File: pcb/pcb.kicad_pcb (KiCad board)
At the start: 2 copper layers, 109 x 54 mm, 60 parts, among them J1 MALE, J10 TC2030_NL, J101 MALE, J102 FEMALE, J103 MALE, J104 FEMALE, J105 MALE, J106 FEMALE, J107 MALE, J108 FEMALE, J11 STANDOFF, J111 STANDOFF, J112 STANDOFF, J113 STANDOFF, J114 STANDOFF, J12 STANDOFF, J13 STANDOFF, J14 STANDOFF, J2 FEMALE, J3 MALE, J4 FEMALE, J5 MALE, J6 FEMALE, J7 MALE, J8 FEMALE, J9 DTR, Q1 2N3904, SW1 ACTION, SW2 ACTION, SW3 ACTION, SW4 ACTION, U3 ATmega328P-MU, Y1 YSX321SL

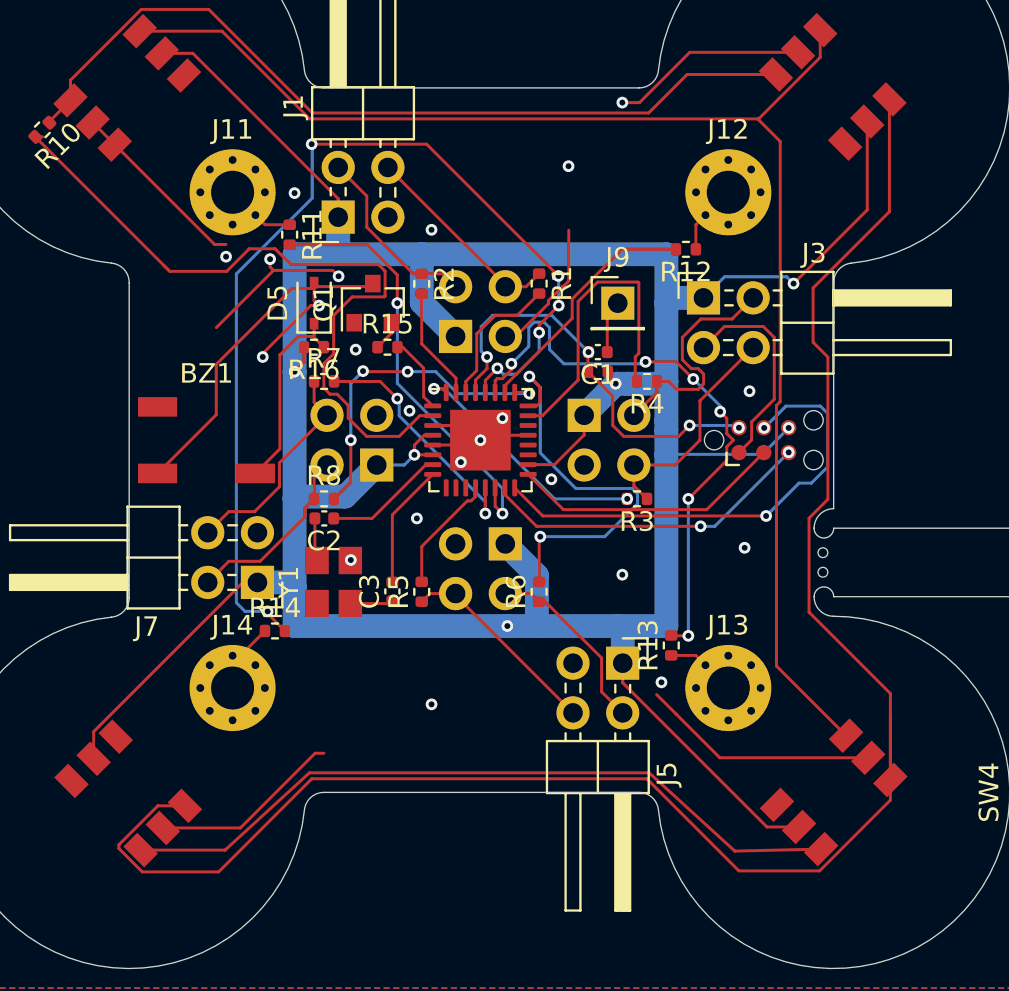
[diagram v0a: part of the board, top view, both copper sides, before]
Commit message: Fix: Tag-Connect cannot be pushed through holes
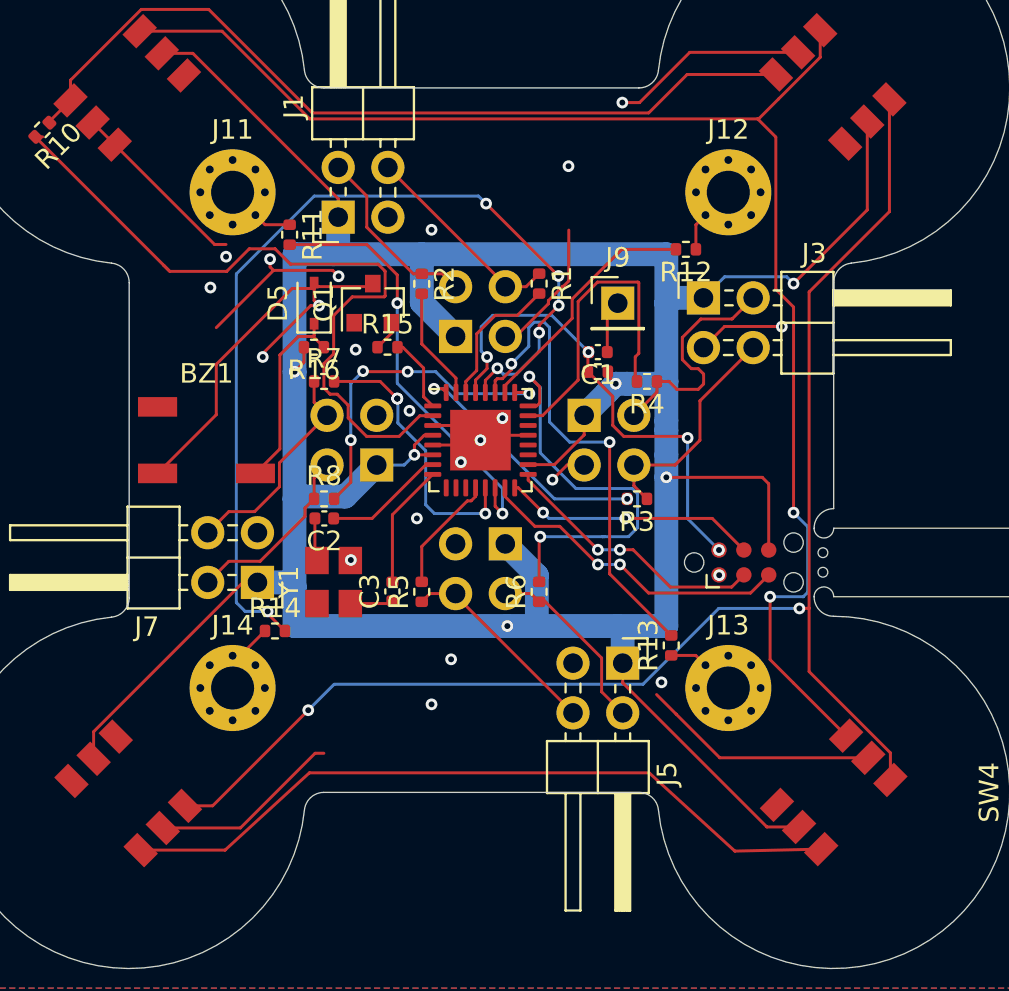
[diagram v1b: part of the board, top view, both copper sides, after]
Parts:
- moved J10 6.33 mm to (134.5, 111.2)
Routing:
- net Net-(D2-Pad3): track 92.9 -> 74.3 mm, vias 0 -> 2
- net /Bottom/MISO: track 24.2 -> 13.0 mm
- net Net-(R13-Pad2): track 30.5 -> 25.0 mm, vias 6 -> 2
- net GNDB: track 75.5 -> 71.0 mm, vias 19 -> 20
- net Net-(R14-Pad2): track 52.1 -> 48.3 mm
- net /Bottom/~RST: track 21.5 -> 25.0 mm
- net Net-(D1-Pad3): track 72.9 -> 75.3 mm, vias 0 -> 2
- net +5VB: track 175.7 -> 177.6 mm
- net Net-(R7-Pad2): track 12.6 -> 14.3 mm, vias 2 -> 3
- net Net-(R6-Pad2): track 20.7 -> 21.5 mm
- net /Bottom/MOSI: track 17.1 -> 16.3 mm
- net /Bottom/SCK: track 14.0 -> 13.8 mm, vias 0 -> 2
- net Net-(J11-Pad1): vias 1 -> 0

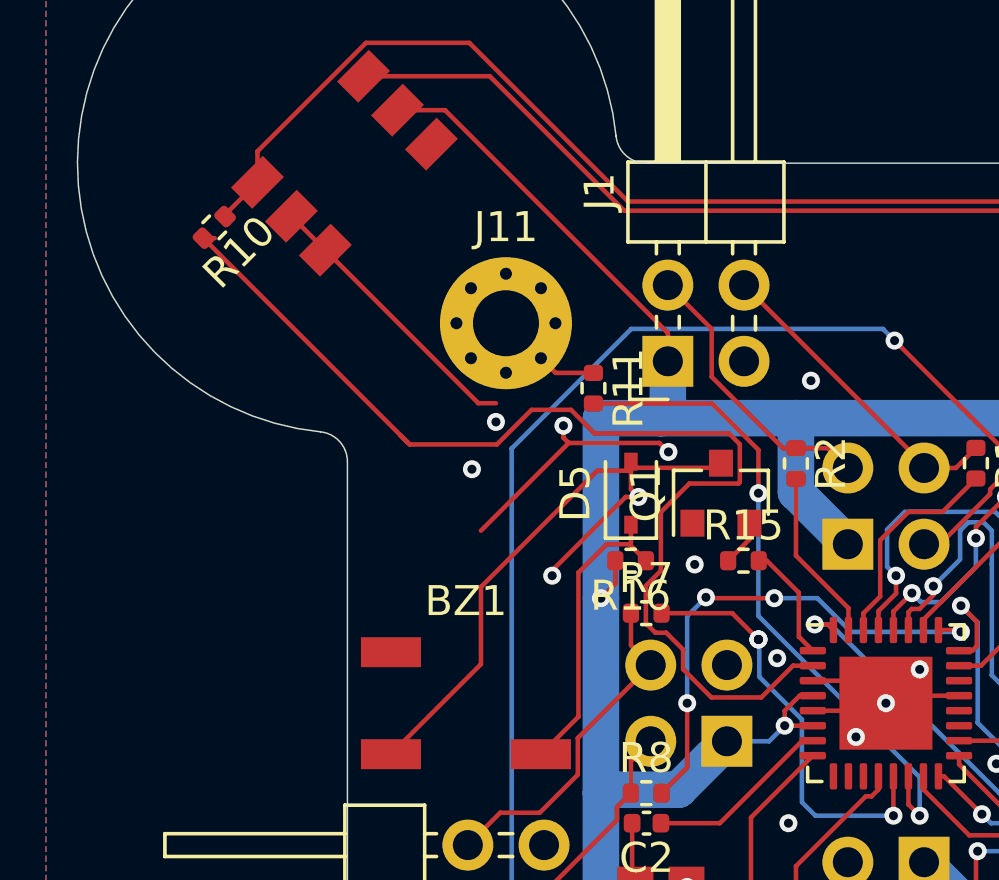
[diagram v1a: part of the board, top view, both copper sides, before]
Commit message: Fix: Small resistor not in solder mask area
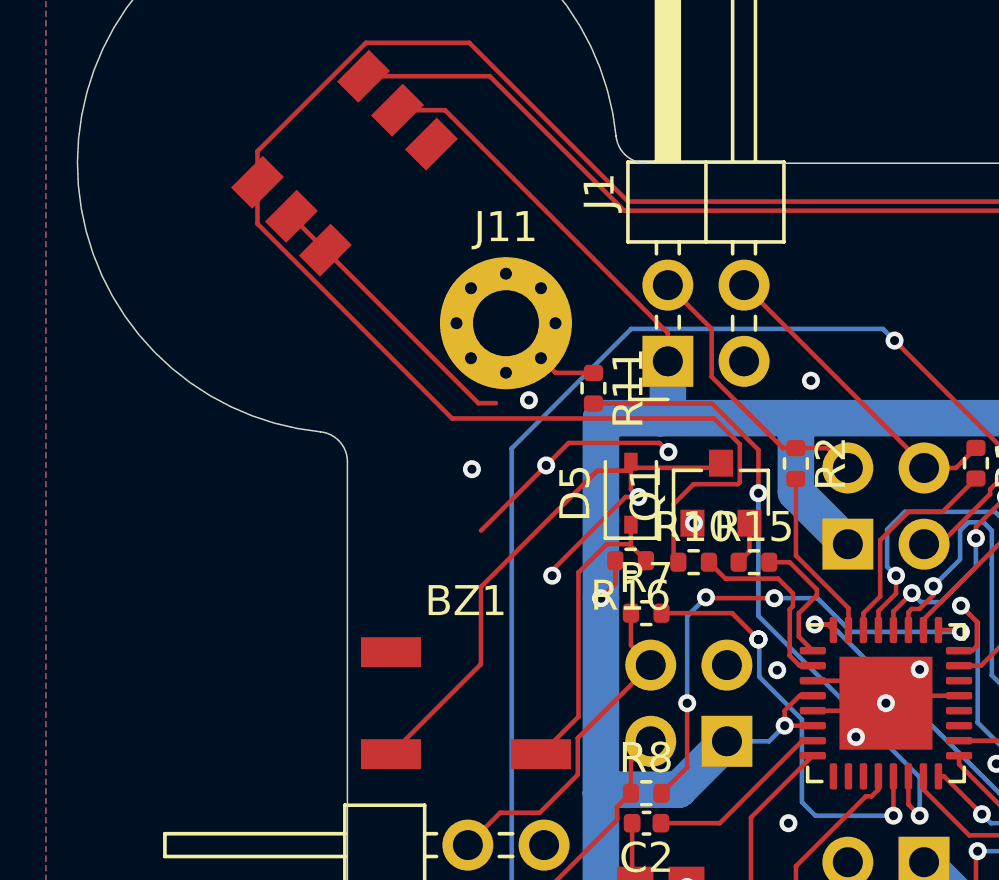
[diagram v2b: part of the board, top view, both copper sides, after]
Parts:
- moved R10 19.5 mm to (114.6, 100.3), turned to 0 degrees
- moved R15 0.35 mm to (116.6, 100.3)
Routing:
- net Net-(R10-Pad2): track 38.1 -> 6.26 mm
- net /Bottom/DIN: track 43.2 -> 67.9 mm
- net GNDB: track 71.0 -> 70.3 mm
- net /Bottom/BUZZER: track 3.90 -> 4.45 mm

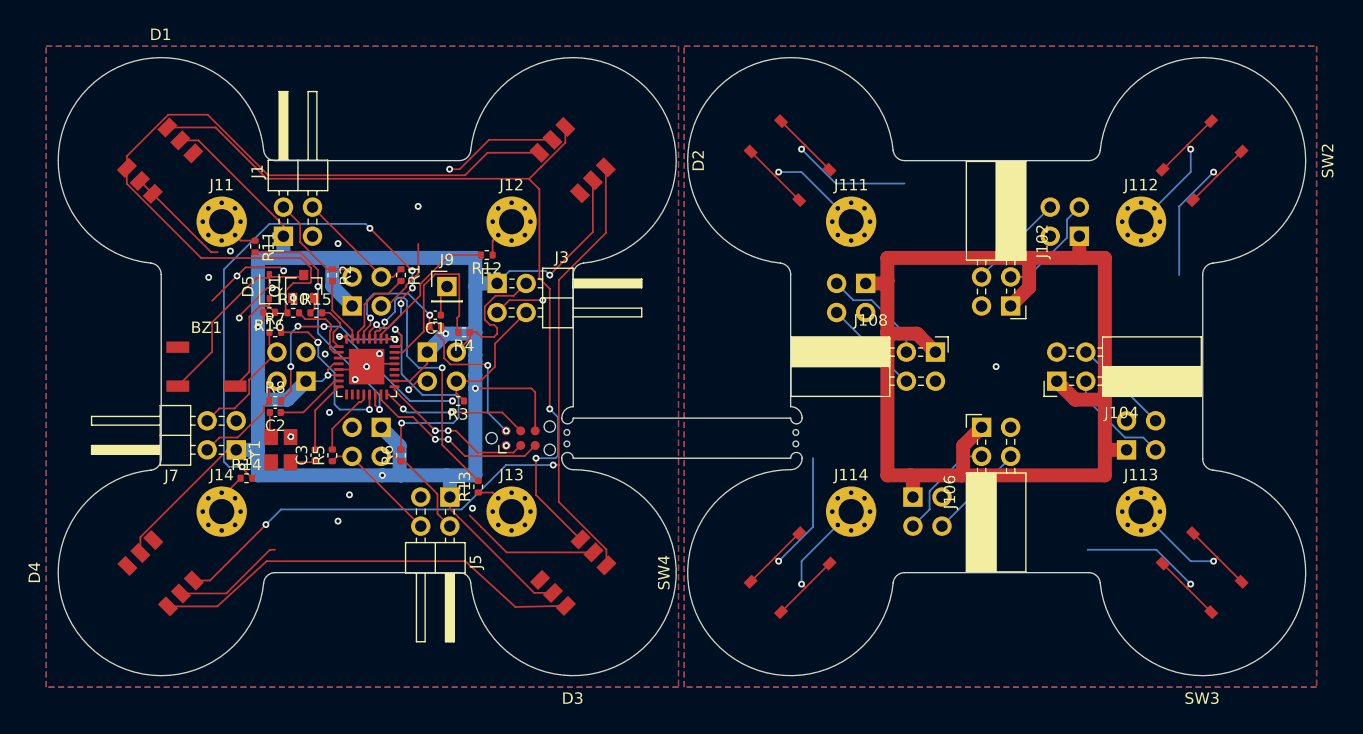
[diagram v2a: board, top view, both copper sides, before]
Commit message: Move holes for headers 0.1 mm inwards
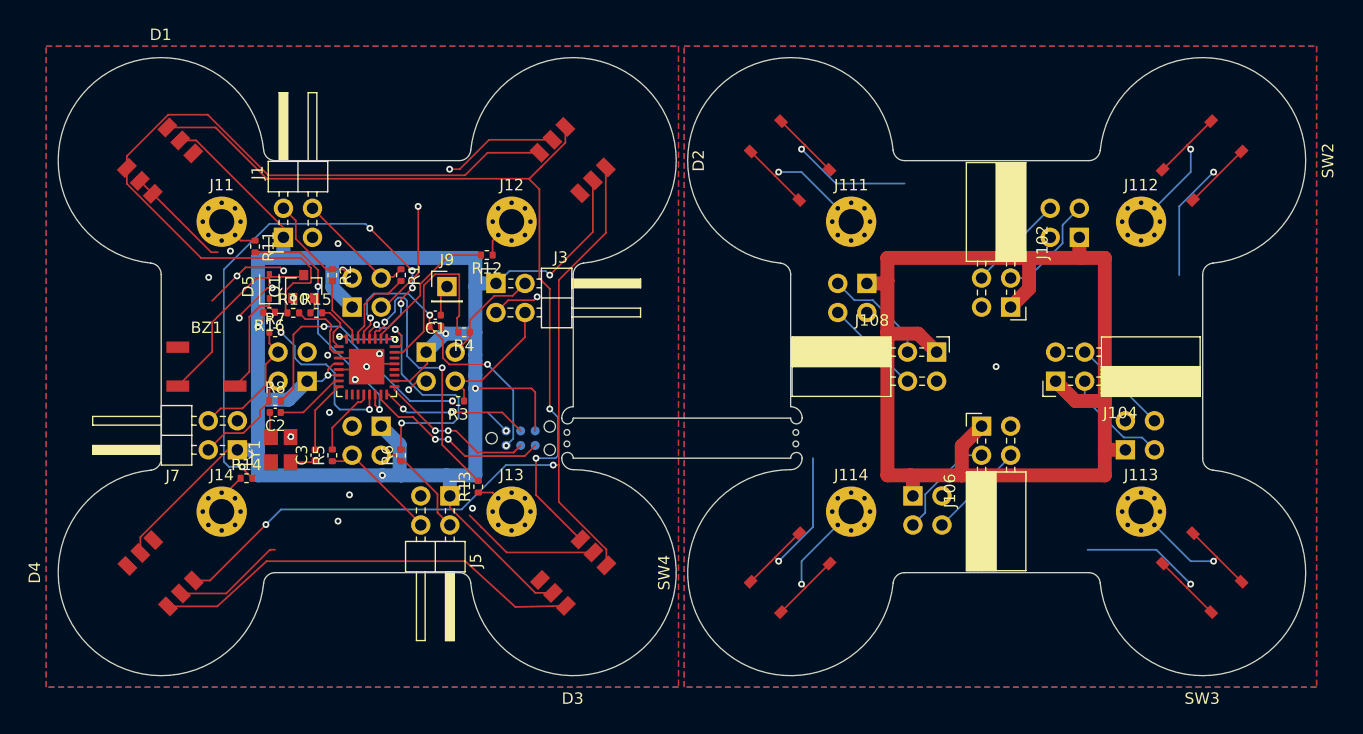
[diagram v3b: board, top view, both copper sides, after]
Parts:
- J10: moved to B.Cu
- moved J104 0.10 mm to (181.2, 106.3)
- moved J108 0.10 mm to (170.8, 103.7)
- moved J1 0.10 mm to (113.7, 93.7)
- moved J101 0.10 mm to (183.3, 93.7)
- moved J102 0.10 mm to (177.3, 99.8)
- moved J103 0.10 mm to (187.3, 112.3)
- moved J105 0.10 mm to (168.7, 116.3)
- moved J106 0.10 mm to (174.7, 110.2)
- moved J107 0.10 mm to (164.7, 97.7)
- moved J2 0.10 mm to (119.7, 99.8)
- moved J3 0.10 mm to (132.3, 97.7)
- moved J4 0.10 mm to (126.2, 103.7)
- moved J5 0.10 mm to (128.3, 116.3)
- moved J6 0.10 mm to (122.3, 110.2)
- moved J7 0.10 mm to (109.7, 112.3)
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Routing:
- net GNDB: track 70.3 -> 76.3 mm
- net /Bottom/TX2: track 12.5 -> 9.54 mm
- net /Bottom/~RST: track 25.0 -> 26.9 mm
- net +5VB: track 177.6 -> 178.1 mm
- net Net-(R7-Pad2): track 14.3 -> 14.1 mm, vias 3 -> 2
- net Net-(R8-Pad2): track 16.9 -> 16.7 mm, vias 4 -> 2

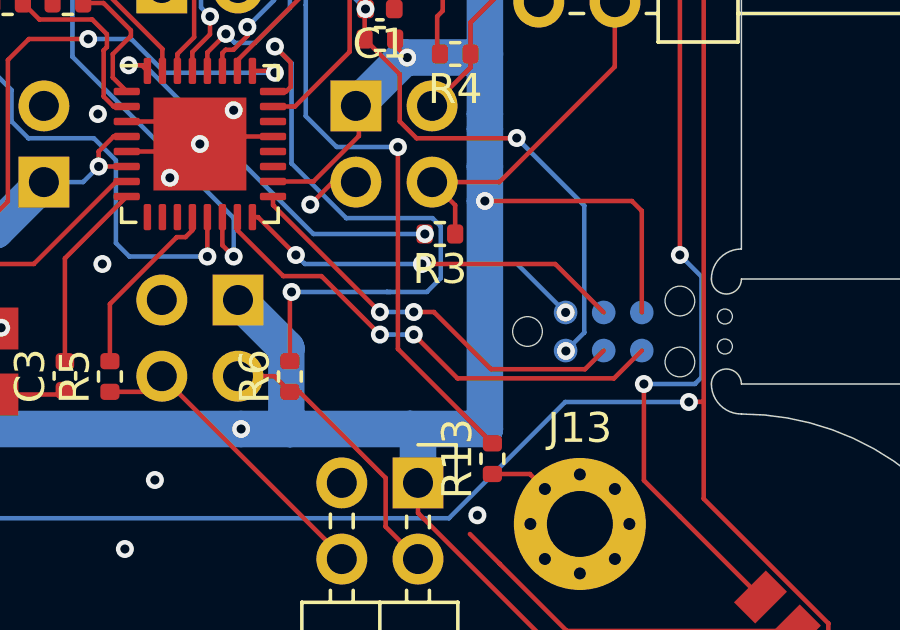
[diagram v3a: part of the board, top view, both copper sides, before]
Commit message: Make Tag-Connect easier accessible
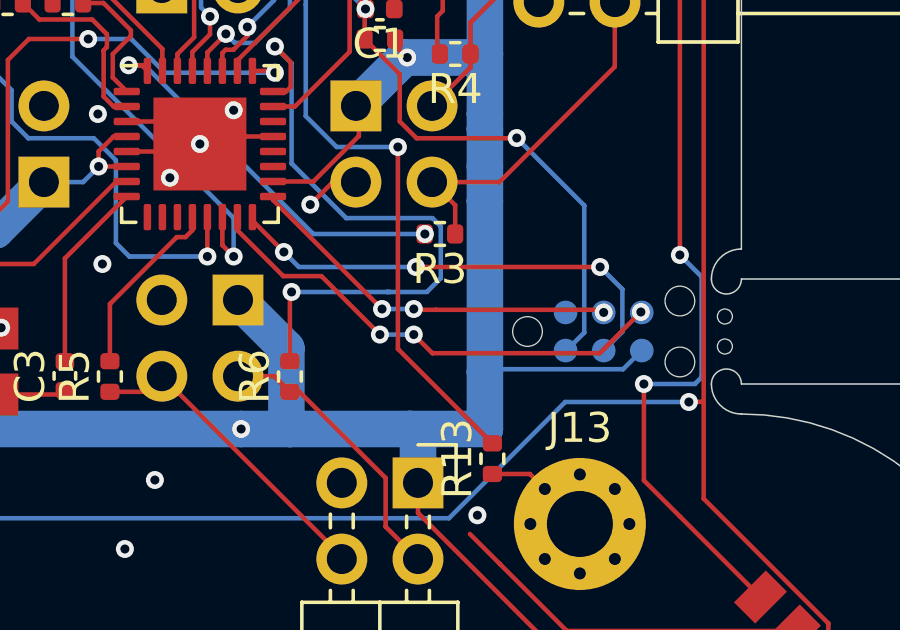
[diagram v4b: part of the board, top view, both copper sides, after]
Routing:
- net +5VB: track 178.1 -> 174.9 mm, vias 6 -> 5
- net /Bottom/MISO: track 13.0 -> 15.7 mm, vias 2 -> 3
- net GNDB: track 76.3 -> 74.0 mm, vias 20 -> 19
- net /Bottom/SCK: track 13.8 -> 12.7 mm, vias 2 -> 3
- net /Bottom/MOSI: track 16.3 -> 16.2 mm, vias 2 -> 3
- net /Bottom/~RST: vias 4 -> 3

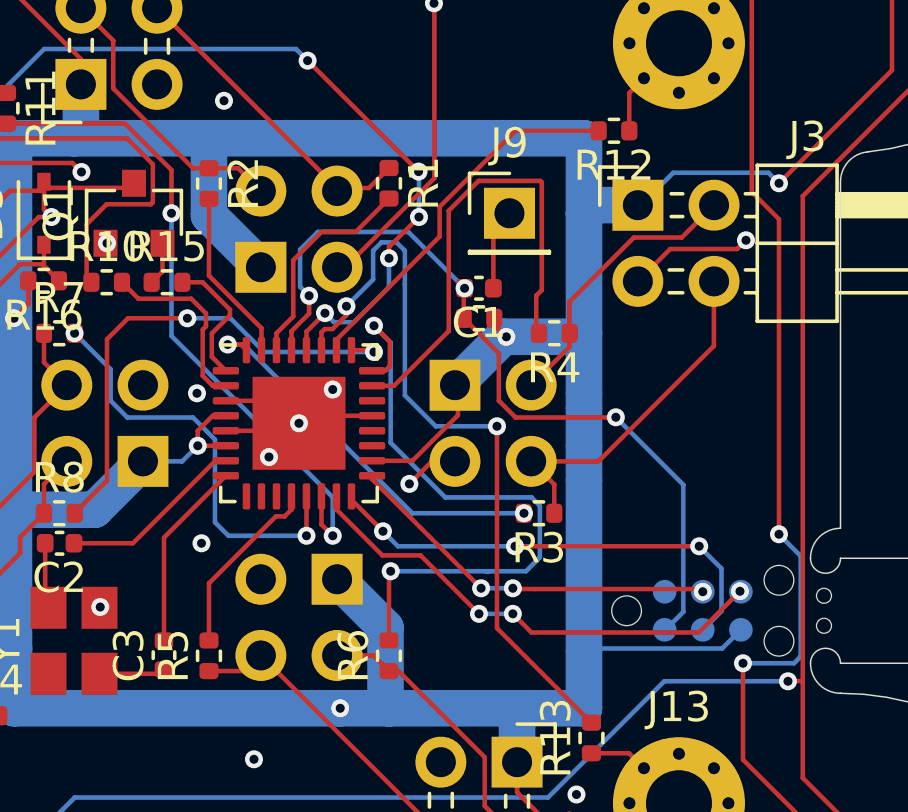
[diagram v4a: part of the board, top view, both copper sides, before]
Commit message: Fix: DRC errors
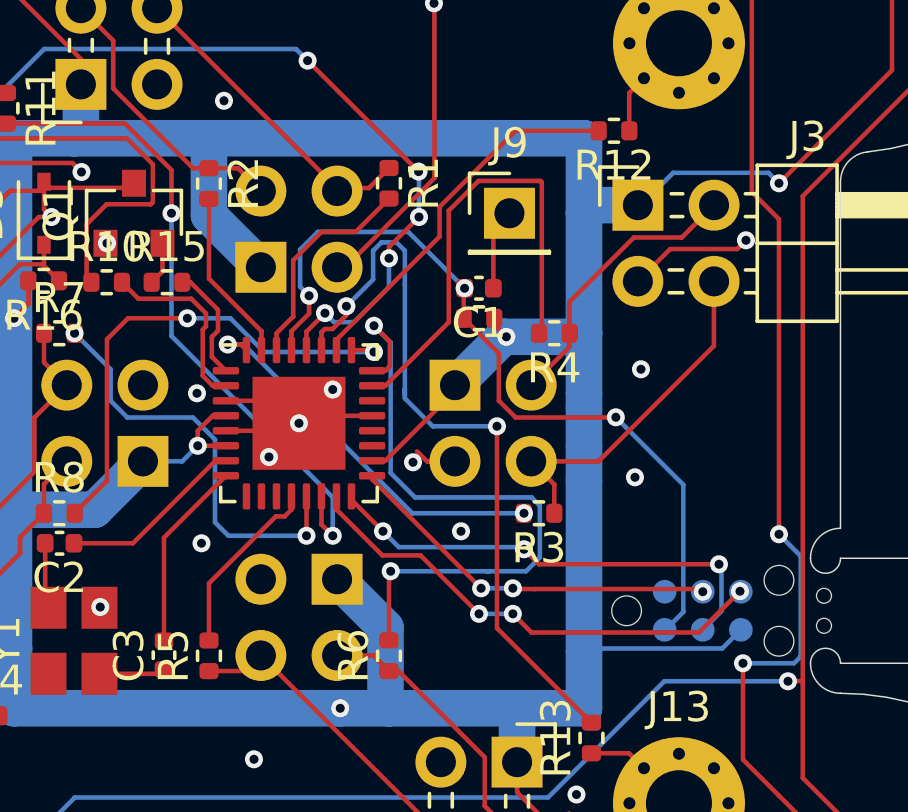
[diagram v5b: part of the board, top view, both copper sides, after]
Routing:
- net Net-(R6-Pad2): track 21.5 -> 22.1 mm
- net +5VB: track 174.9 -> 174.3 mm
- net /Bottom/BUZZER: track 4.45 -> 3.88 mm
- net GNDB: track 74.0 -> 74.4 mm, vias 19 -> 22
